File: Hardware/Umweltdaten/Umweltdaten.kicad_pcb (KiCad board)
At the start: 2 copper layers, 50 x 50 mm, 31 parts, among them IC1 ATMEGA328P-A, IC3 GY88, P1 BATT, P10 I2C, P11 microSD_SPI, P2 ISP, P3 RS232, P4 Port B, P5 Port C, P6 Port D, P7 ADC, P8 I2C, P9 I2C, U1 TLV70233DBV, Y1 Crystal 16Mhz

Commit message: finish schema and PCB
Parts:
- added J1: RESET, Wire_Connections_Bridges:WireConnection_0.8mmPad, B.Cu at (118.8, 66.4)
- added REF**: MountingHole_2-7mm, Mounting_Holes:MountingHole_2-7mm, F.Cu at (145.0, 55.0)
- added REF**: MountingHole_2-7mm, Mounting_Holes:MountingHole_2-7mm, F.Cu at (105.0, 95.0)
- JP2: moved to B.Cu
- P4: footprint Pin_Headers:Pin_Header_Straight_1x08 -> Pin_Headers:Pin_Header_Straight_1x06
- moved P4 97.6 mm to (117.8, 77.9), turned to 90 degrees
- moved JP2 97.2 mm to (130.8, 95.6), turned to 90 degrees
- moved P8 88.9 mm to (138.1, 65.2)
- moved IC3 87.0 mm to (134.3, 98.3)
- moved P9 81.1 mm to (143.2, 65.2)
- moved P6 78.3 mm to (120.3, 52.5), turned to 270 degrees
- moved P10 73.7 mm to (148.3, 65.2)
- moved P5 69.6 mm to (140.6, 52.5), turned to 270 degrees
- moved R2 38.6 mm to (112.8, 94.0)
- moved R5 38.6 mm to (110.8, 94.0)
- moved R4 35.1 mm to (110.8, 89.2)
- moved R3 31.2 mm to (112.8, 89.2)
- moved C9 30.9 mm to (112.8, 84.4), turned to 270 degrees
- moved R1 30.9 mm to (110.8, 84.4), turned to 90 degrees
- moved Y1 17.1 mm to (107.6, 78.4)
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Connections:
- net PB4 renamed MISO
- net PC5 renamed SCL
- net PD1 renamed TX
- net SS renamed PB2
- C7 pad 1: XTAL1 -> PB6
- IC1 pad 7: XTAL1 -> PB6
- IC3 pad 7: Net-(IC3-Pad7) -> GND
- IC3 pad 8: PD5 -> PD7
- JP1 pad 2: Net-(JP1-Pad2) -> +BATT
- JP2 pad 2: Net-(IC3-Pad7) -> GND
- P10 pad 4: PD4 -> /connector/O.S._3
- P8 pad 4: PD2 -> /connector/O.S._1
- P9 pad 4: PD3 -> /connector/O.S._2
- U1 pad 3: Net-(JP1-Pad2) -> +BATT
- Y1 pad 1: XTAL1 -> PB6
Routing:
- net GND: track 164.1 -> 243.0 mm, vias 11 -> 10
- net PD7: track 0.00 -> 73.5 mm, vias 0 -> 3
- net SDA: track 0.00 -> 73.1 mm, vias 0 -> 1
- net SCL: track 0.00 -> 69.1 mm, vias 0 -> 1
- net PD6: track 0.00 -> 65.5 mm, vias 0 -> 3
- net +3V3: track 98.2 -> 148.6 mm
- net ADC6: track 0.00 -> 25.4 mm, vias 0 -> 1
- net PD5: track 0.00 -> 24.3 mm, vias 0 -> 1
- net PC0: track 0.00 -> 22.2 mm
- net PC6: track 5.64 -> 27.5 mm, vias 0 -> 1
- net PB3: track 23.9 -> 45.2 mm, vias 0 -> 1
- net ADC7: track 0.00 -> 20.4 mm
- net PC1: track 0.00 -> 20.0 mm
- net PC2: track 0.00 -> 17.6 mm
- net PC3: track 0.00 -> 16.7 mm
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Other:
- board text added: "GND"
- board text added: "RX"
- board text added: "TX"

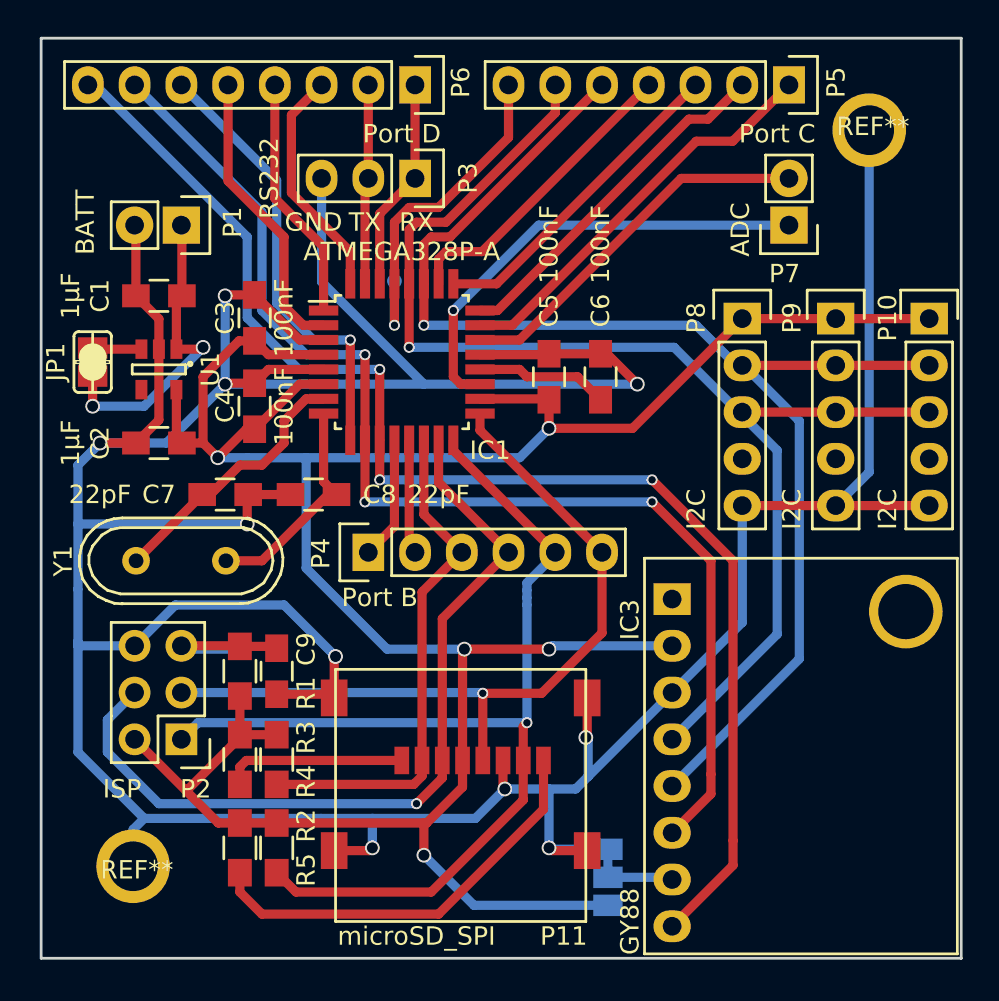
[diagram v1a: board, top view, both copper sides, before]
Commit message: add silkscreen and fix DRC errors
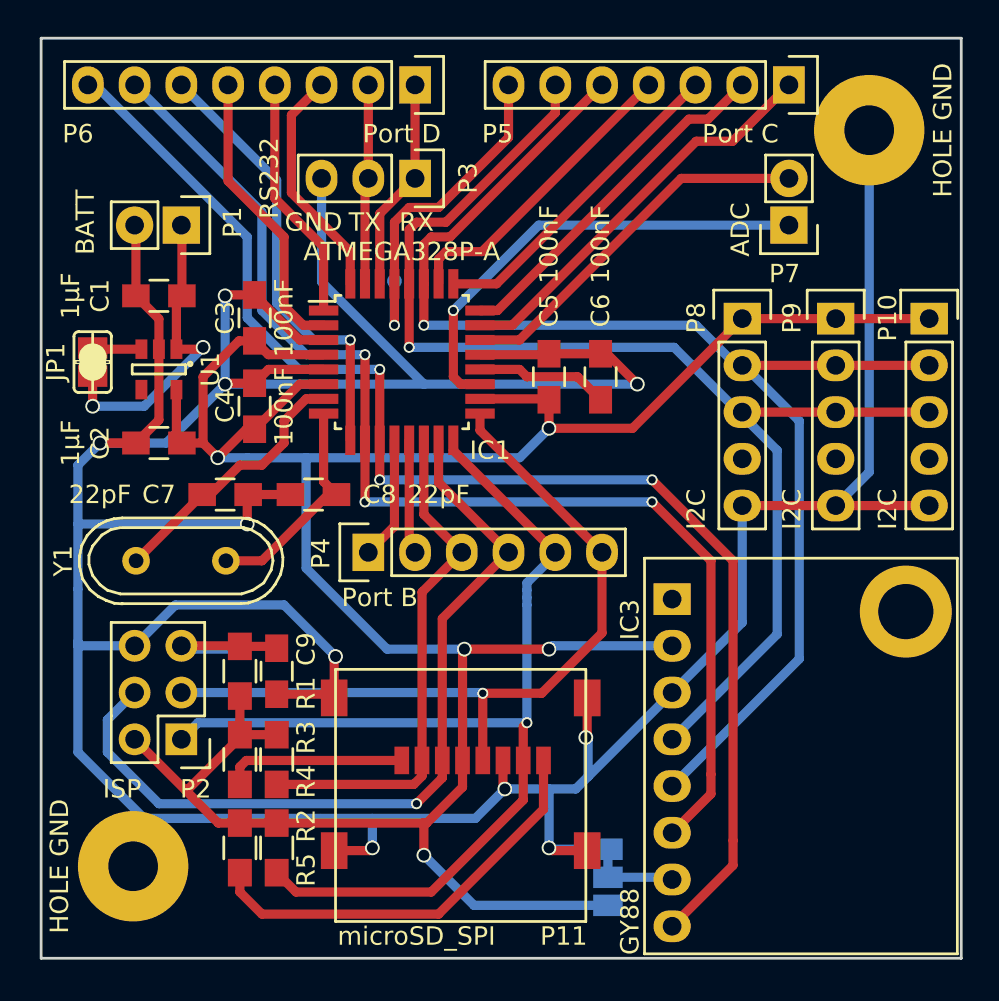
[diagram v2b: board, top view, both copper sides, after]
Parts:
- HOLE GND: renamed from REF** (x2)
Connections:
- IC3 pad : (no net) -> GND
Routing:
- added copper zone on B.Cu, net GND
- added copper zone on F.Cu, net GND
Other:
- board text added: "RESET"
- board text added: "UgoesSky Datalogger"

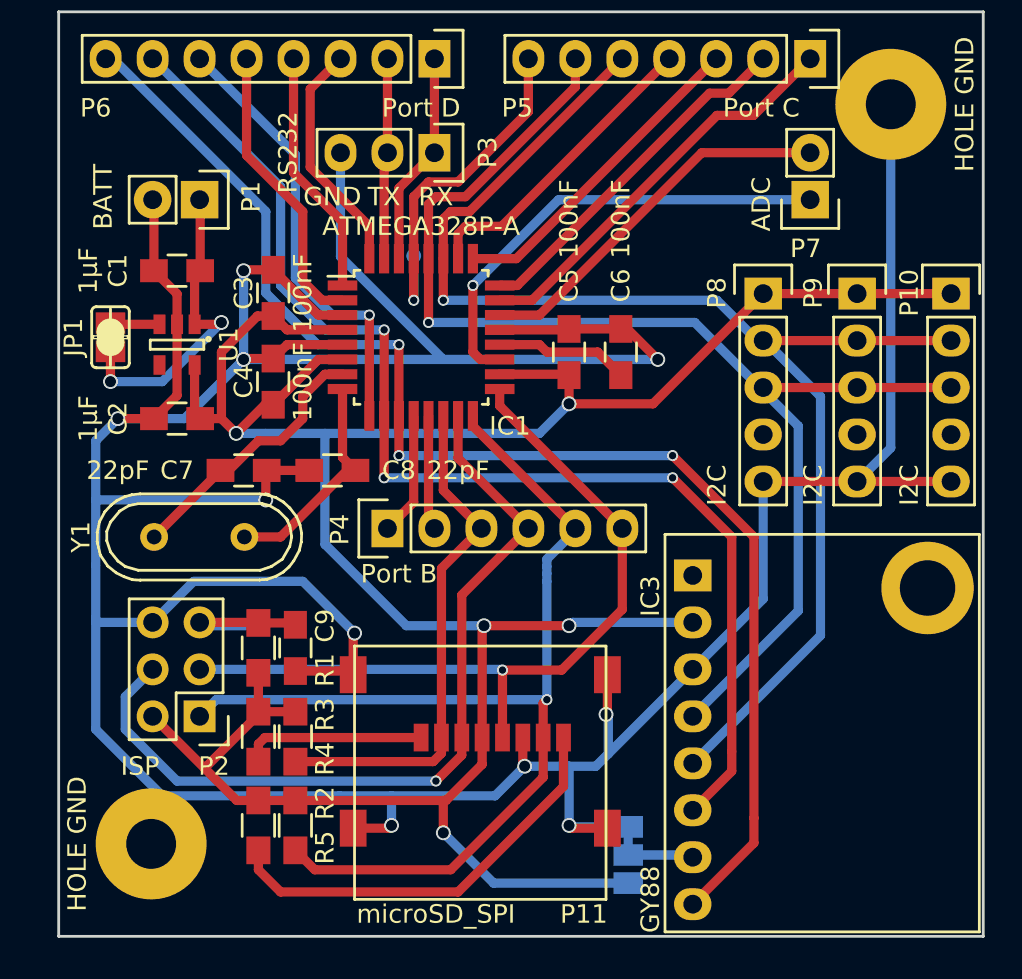
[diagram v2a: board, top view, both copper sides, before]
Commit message: add logos and bom
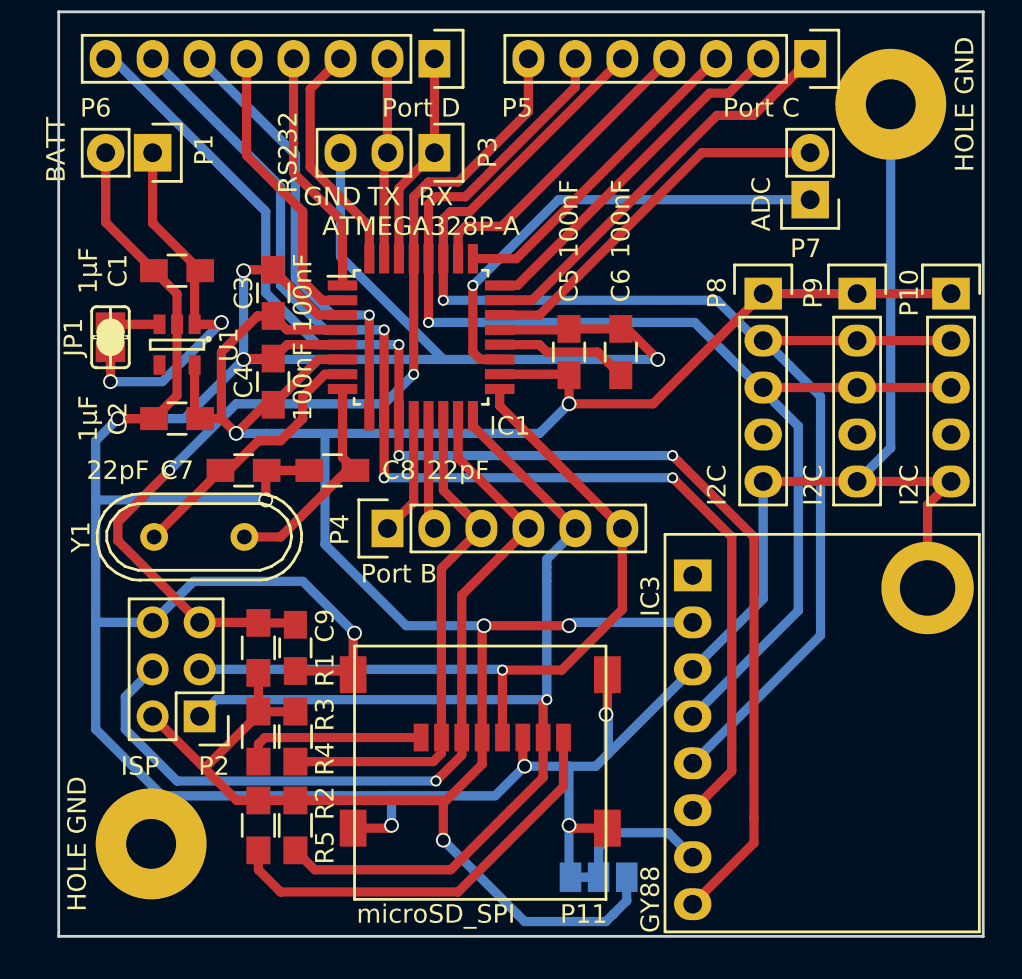
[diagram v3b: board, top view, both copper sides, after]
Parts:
- removed J1: RESET, Wire_Connections_Bridges:WireConnection_0.8mmPad
- added G***: LOGO, LOGO:AUB, B.Cu at (120.4, 88.8)
- added G***: LOGO, LOGO:UgoesSky_klein, B.Cu at (101.2, 67.6)
- moved P1 3.59 mm to (105.1, 57.6)
- moved JP2 2.00 mm to (129.2, 96.8), turned to 180 degrees
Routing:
- net PC6: track 27.5 -> 52.4 mm, vias 1 -> 2
- net GND: track 243.0 -> 256.5 mm
- net +BATT: track 21.5 -> 25.1 mm
- net +3V3: track 148.6 -> 151.4 mm
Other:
- board text added: "U1L"
- board text added: "UgoesSky Datalogger V2"
- board text removed: "RESET"
- board text removed: "UgoesSky Datalogger"
